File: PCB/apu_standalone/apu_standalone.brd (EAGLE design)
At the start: 110.5 x 54.4 mm, 95 parts, among them IC1 74AHC573, IC10 DAC, IC11 IS62C1024AL, IC12 ATMEGA2560, IC15 FT232RL, IC2 4050D, IC3 DS1307, IC4 LP298XS, IC5 S-SMP, IC6 S-DSP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

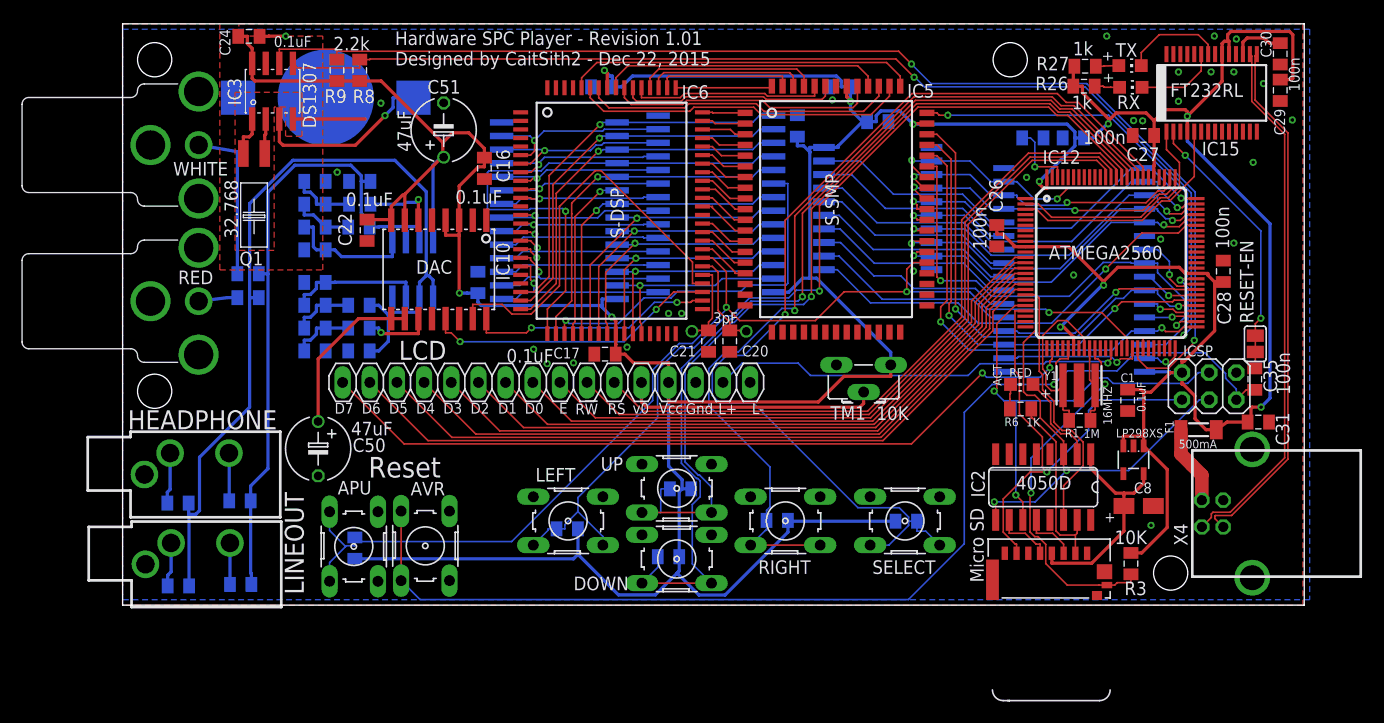
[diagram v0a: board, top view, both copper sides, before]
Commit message: PC Side communications
Added various commands for a planned total rewrite of the PC side
client,.
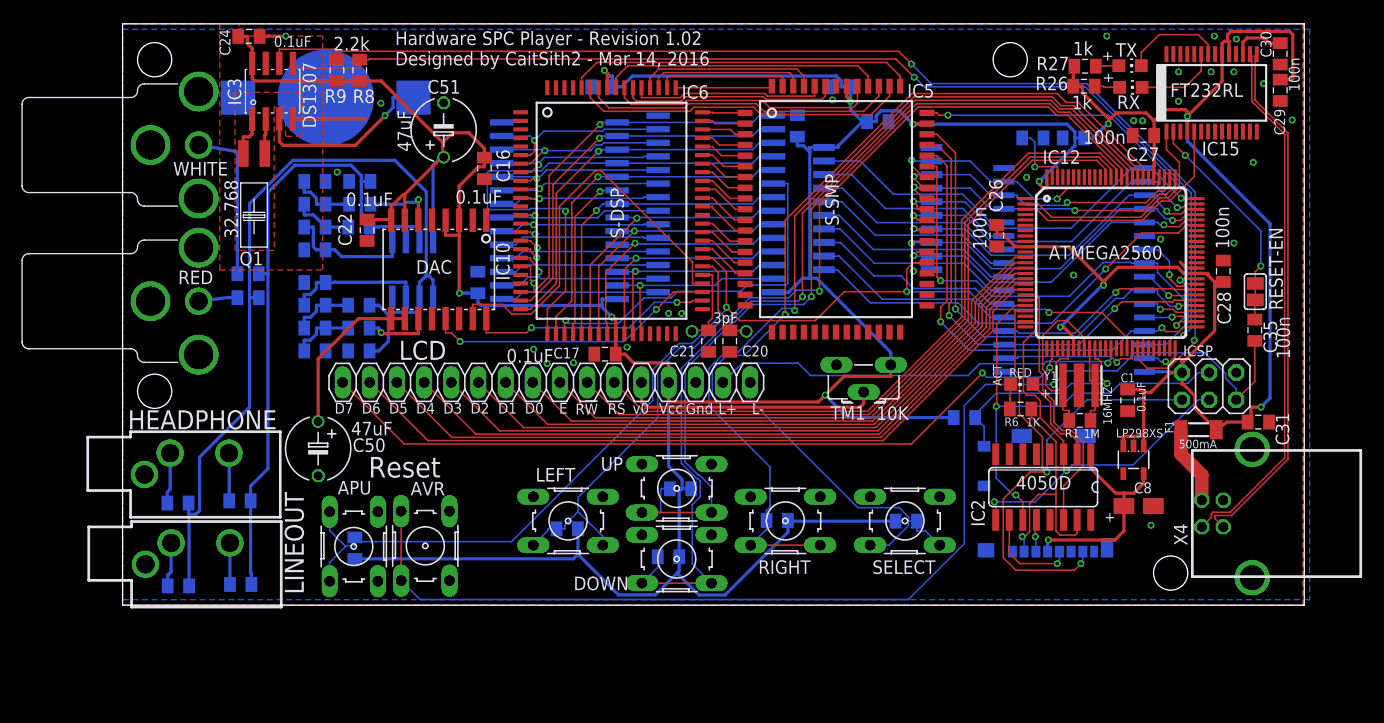
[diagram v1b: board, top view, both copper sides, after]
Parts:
- X1: value MICROSDMOLEX -> MICROSDMOLEX-2; device adafruit:MICROSD-1 -> adafruit:MICROSD-2
- moved R3 20.7 mm to (78.7, 17.5), flipped to the bottom, turned to 180 degrees
- moved X1 10.4 mm to (86.3, 9.86), flipped to the bottom
- moved RESET-EN 4.88 mm to (105.9, 29.3)
- moved C35 4.57 mm to (105.9, 25.7)
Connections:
- net CD: now also X1.CD1; no longer X1.11
- net GND: now also X1.CD2, X1.G1, X1.G2, X1.G3; no longer X1.12, X1.9
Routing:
- net CD: track 34.0 -> 20.8 mm, vias 2 -> 1
- net DO: track 45.0 -> 54.3 mm, vias 1 -> 2
- net BUF_CS: track 17.6 -> 23.7 mm, vias 0 -> 1
- net DTR: track 25.8 -> 21.2 mm
- net RESET: track 111.4 -> 115.9 mm
- net BUF_CLK: track 5.40 -> 9.19 mm, vias 0 -> 1
- net BUF_DI: track 5.06 -> 3.03 mm, vias 0 -> 1
- net GND: track 9.20 -> 11.0 mm
- net DI: track 43.2 -> 44.2 mm
- net VCC: track 468.6 -> 468.0 mm, vias 11 -> 12
- net +3V3: track 21.0 -> 20.6 mm, vias 0 -> 1
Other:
- board text added: "Hardware SPC Player - Revision 1.02 Designed by CaitSith2 - Mar 14, 2016"
- board text removed: "Hardware SPC Player - Revision 1.01 Designed by CaitSith2 - Dec 22, 2015"

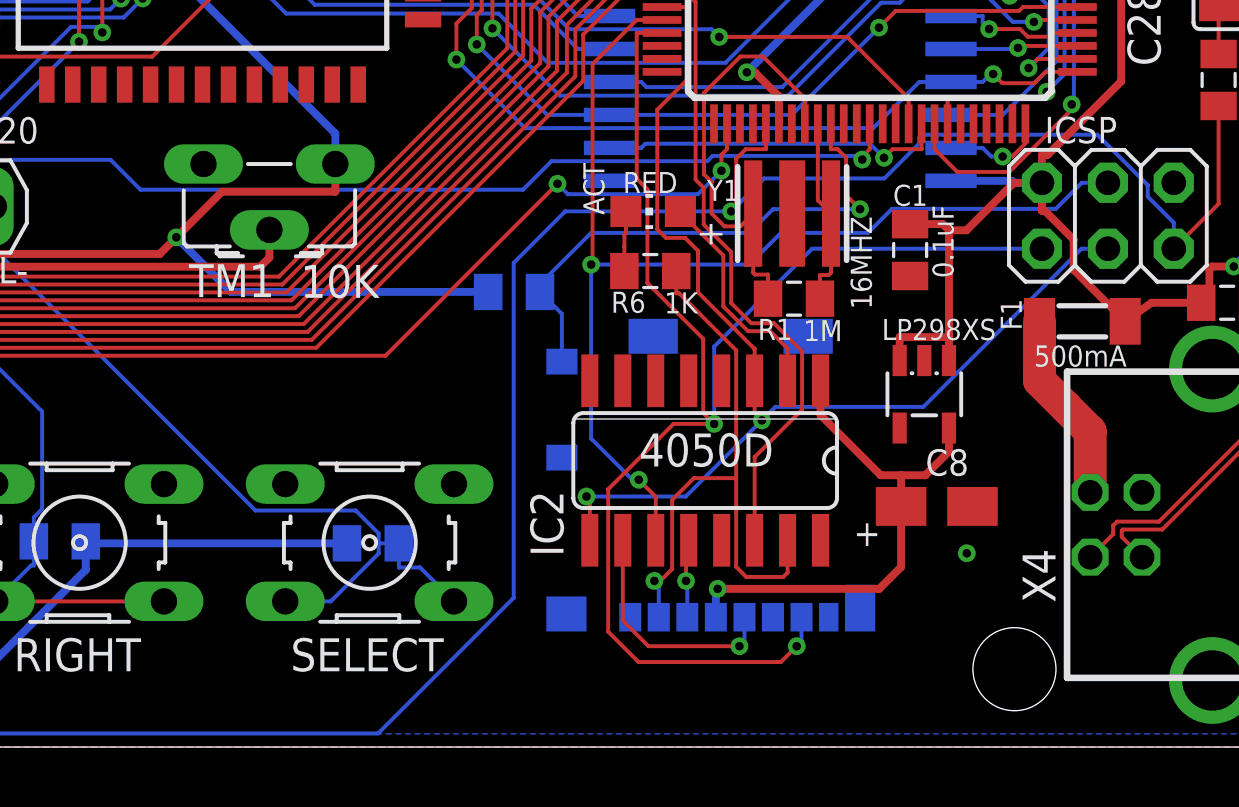
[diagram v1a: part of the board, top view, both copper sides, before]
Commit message: Changed micro-SD holder to push-in-push-out type.
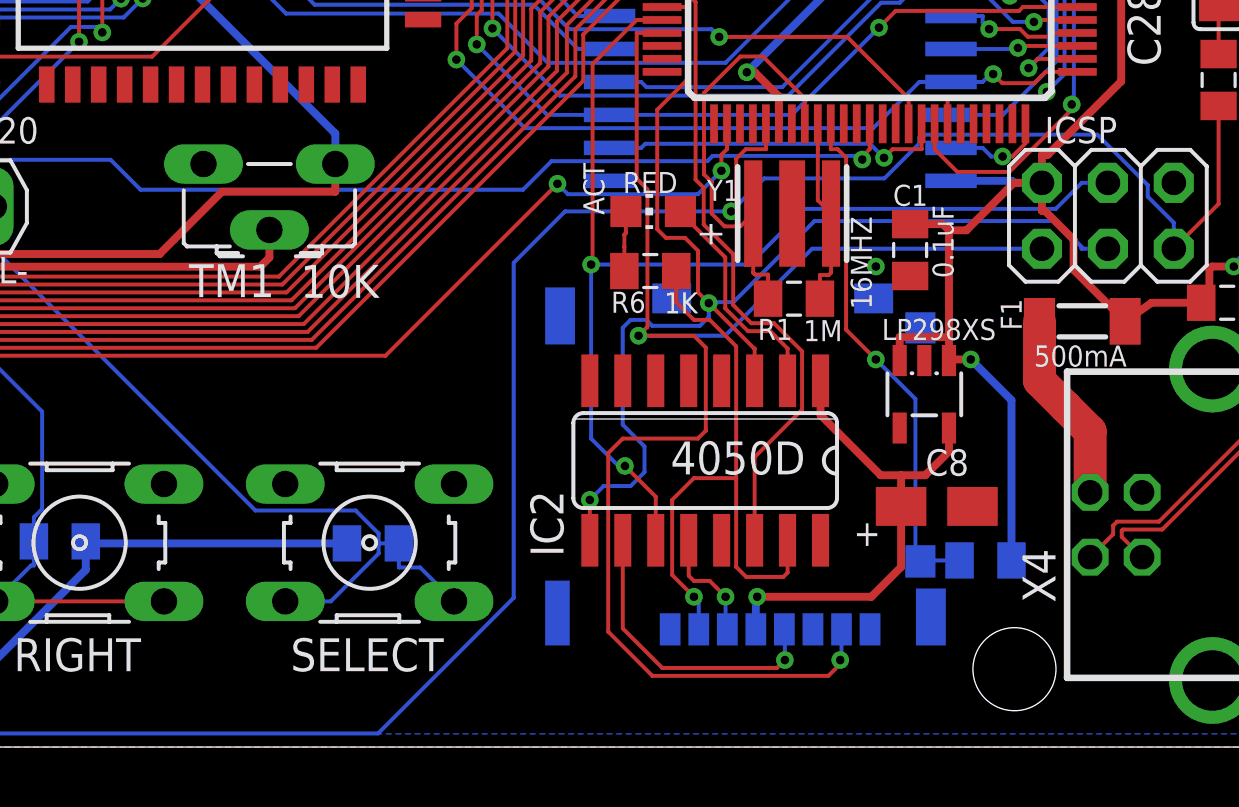
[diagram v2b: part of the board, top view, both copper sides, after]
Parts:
- removed X1: MICROSDMOLEX-2, adafruit:MICROSD-2
- added U$1: MICROSD-2, adafruit:MICROSD-3
- moved R3 20.9 mm to (96.9, 7.19), turned to 0 degrees
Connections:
- net +3V3: now also U$1.4; no longer X1.4
- net BUF_CLK: now also U$1.5; no longer X1.5
- net BUF_CS: now also U$1.2; no longer X1.2
- net BUF_DI: now also U$1.3; no longer X1.3
- net CD: now also U$1.CD_SWITCH; no longer X1.CD1
- net DO: now also U$1.7; no longer X1.7
- net GND: now also U$1.6, U$1.CD_GND, U$1.G1, U$1.G2, U$1.G3, U$1.G4, U$1.G5; no longer X1.6, X1.CD2, X1.G1, X1.G2, X1.G3
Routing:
- net CLK: track 45.3 -> 49.3 mm
- net DO: track 54.3 -> 58.1 mm
- net VCC: track 468.0 -> 464.4 mm
- net BUF_CLK: track 9.19 -> 11.6 mm
- net BUF_DI: track 3.03 -> 4.41 mm
- net +3V3: track 20.6 -> 19.3 mm
- net CD: track 20.8 -> 20.0 mm
- net BUF_CS: track 23.7 -> 24.4 mm

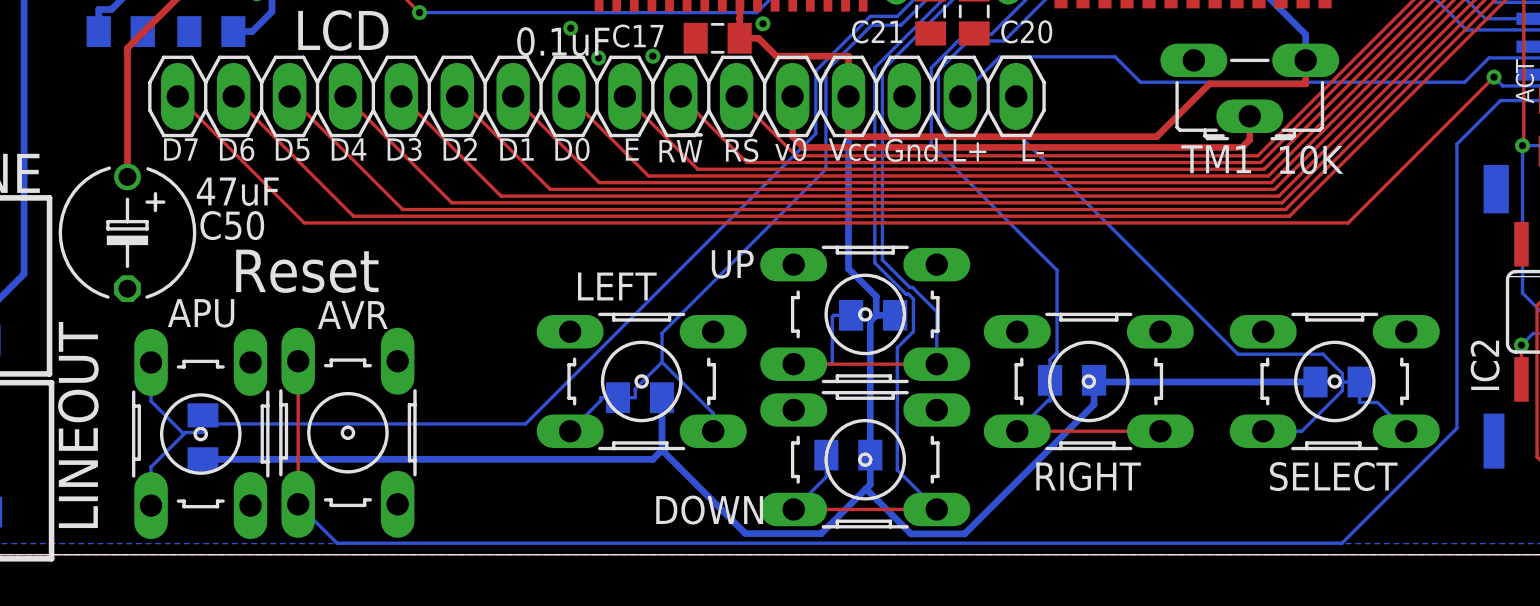
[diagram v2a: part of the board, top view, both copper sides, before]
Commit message: APU reset button now has a 470 ohm series resistor to ground.
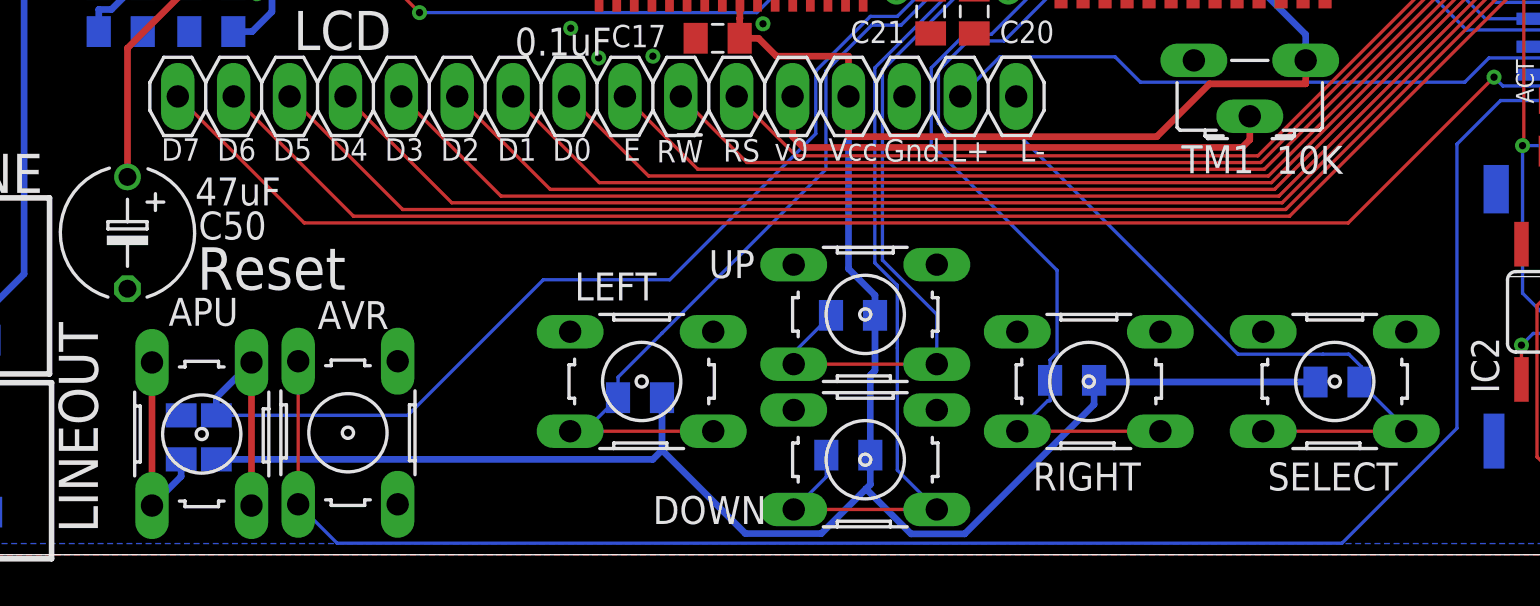
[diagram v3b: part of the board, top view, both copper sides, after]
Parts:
- added R14: 470, adafruit:R0805
- moved R12 0.91 mm to (51.3, 10.9)
- moved R2 0.61 mm to (22.3, 5.33)
- turned APU to 90 degrees
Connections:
- new net N$5: APU.1, APU.2, R14.2
- net GND: now also R14.1; no longer APU.1, APU.2
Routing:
- net N$5: track 0.00 -> 9.15 mm
- net UP: track 85.4 -> 83.5 mm
- net LEFT: track 87.7 -> 89.6 mm
- net SELECT: track 94.9 -> 96.5 mm
- net VCC: track 464.4 -> 462.8 mm
- net DOWN: track 92.0 -> 91.4 mm
